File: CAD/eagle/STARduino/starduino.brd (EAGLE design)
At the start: 101.6 x 38.1 mm, 119 parts, among them J1 J30J-9J30, J2 MICRO_SD, J3 J30J-15J30, J4 J30J-31J30, J5 RPI-ZERO, J6 RPI-CSI, Q1 FDG8842CZ, Q2 FDG8842CZ, Q5 FDG8842CZ, Q6 FDG8842CZ, T1 750313972, U1 LT8301, U10 MC74VHC1GT125, U11 TCA9535_RTW_24, U12 MAX31725MTA+, U13 BMX055, U14 DRV8846RGER, U15 P82B715, U16 MC74VHC1GT125, U17 PCA9306DCT, U2 LT3465/A, U3 LTC3112FE, U4 DS3231MZ+, U5 MT25QL01GBBB8ESF-0AAT, U6 ATSAMD21G18, U7 MIC5319, U8 ADXL375BCCZ, U9 MC14504BDTG

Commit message: Adjusted some STARduino things
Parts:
- removed R20, R21, R33, R36: 4.7k, resistor:R0603
- added C28: 100nF, resistor:C0603
- added R15: 4.7k, SparkFun-Passives:0603-ARV
- C29: value 4.7uF -> 2.2uF; device resistor:A/3216-18R -> resistor:C0603
- moved C29 62.3 mm to (-10.2, -21.6), turned to 0 degrees
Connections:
- removed net N$1: L3.2, U6.44
- removed net N$2: L4.2, U6.17
- removed net N$3: L5.2, U6.36
- removed net N$4: FB1.2, U6.6
- new net N$10: C19.1, C20.1, C21.1, C22.1, C23.1, C24.1, FB1.2, L3.2, L4.2, L5.2, U6.17, U6.36, U6.44, U6.6
- new net N$9: C28.1, U7.4
- net +3V3: now also C29.1, R15.5, R15.6, R15.7, R15.8; no longer C19.1, C20.1, C21.1, C22.1, C23.1, C24.1, C29.+, R20.2, R21.2, R33.2, R36.2
- net GND: now also C28.2, C29.2; no longer C29.-
- net SCL: now also R15.4; no longer R21.1
- net SCL_BUFF: now also R15.2; no longer R36.1
- net SDA: now also R15.3; no longer R20.1
- net SDA_BUFF: now also R15.1; no longer R33.1
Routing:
- net +3V3: track 259.2 -> 246.5 mm
- net N$4: track 9.40 -> 0.00 mm
- net N$2: track 7.24 -> 0.00 mm, vias 2 -> 0
- net SDA: track 117.0 -> 114.0 mm
- net N$1: track 2.90 -> 0.00 mm
- net N$10: track 0.00 -> 2.04 mm
- net GND: track 71.8 -> 70.5 mm, vias 69 -> 68
- net N$3: track 1.09 -> 0.00 mm
- net SCL: track 136.9 -> 135.9 mm
- net SDA_BUFF: track 52.9 -> 52.1 mm
- net SCL_BUFF: track 51.8 -> 51.0 mm

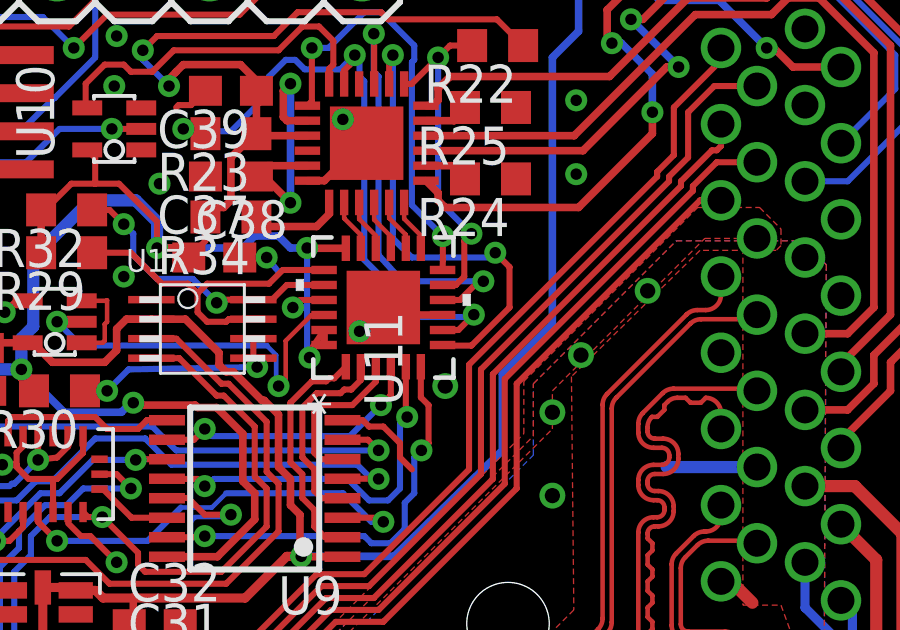
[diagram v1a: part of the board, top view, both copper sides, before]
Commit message: Multiplexer Pinout Change
Small change to multiplexer layout for increased sense-making.
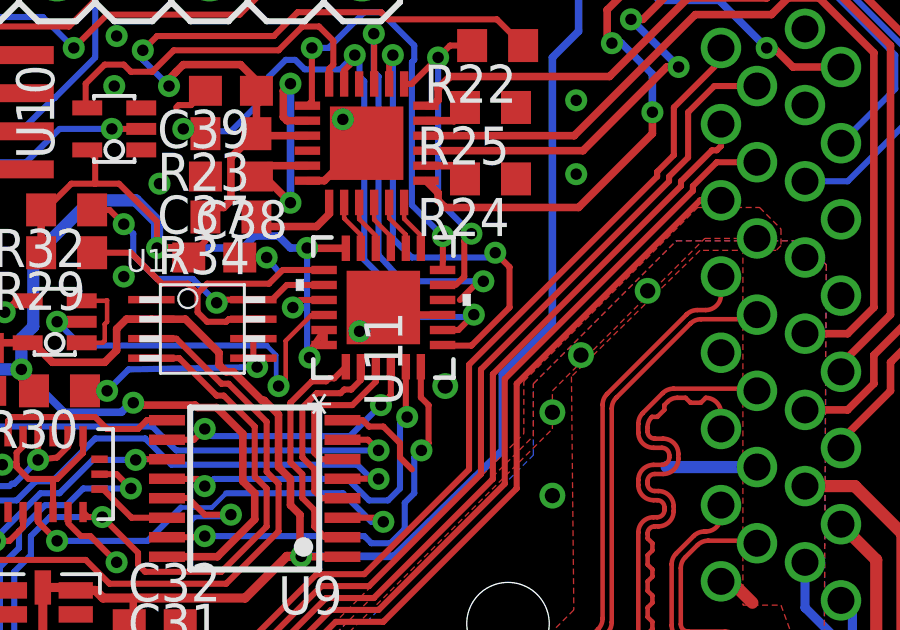
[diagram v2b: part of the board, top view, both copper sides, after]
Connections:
- net M0: now also U11.11; no longer U11.7
- net NFAULT: now also U11.7; no longer U11.11
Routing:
- net M1: track 14.7 -> 14.0 mm
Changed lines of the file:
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@@
 <?xml version="1.0" encoding="utf-8"?>
 <!DOCTYPE eagle SYSTEM "eagle.dtd">
-<eagle version="6.5.0">
+<eagle version="7.5.0">
 <drawing>
 <settings>
@@
 <pass name="Default">
 <param name="RoutingGrid" value="50mil"/>
+<param name="AutoGrid" value="1"/>
+<param name="Efforts" value="0"/>
+<param name="TopRouterVariant" value="1"/>
 <param name="tpViaShape" value="round"/>
 <param name="PrefDir.1" value="|"/>
@@
 <contactref element="U14" pad="7"/>
 <contactref element="R22" pad="2"/>
-<contactref element="U11" pad="11"/>
 <via x="84.93125" y="24.28875" extent="1-16" drill="0.381"/>
 <via x="83.82" y="30.1625" extent="1-16" drill="0.381"/>
 <wire x1="83.82" y1="30.1625" x2="83.82" y2="25.4" width="0.2032" layer="16"/>
 <wire x1="83.82" y1="25.4" x2="84.93125" y2="24.28875" width="0.2032" layer="16"/>
-<wire x1="83.969375" y1="22.5783125" x2="83.9351875" y2="22.5783125" width="0.2032" layer="1"/>
 <wire x1="82.68875" y1="29.28" x2="82.9375" y2="29.28" width="0.2032" layer="1"/>
 <wire x1="82.9375" y1="29.28" x2="83.82" y2="30.1625" width="0.2032" layer="1"/>
 <wire x1="83.82" y1="30.1625" x2="84.216875" y2="30.559375" width="0.2032" layer="1"/>
 <wire x1="84.216875" y1="30.559375" x2="84.954375" y2="30.559375" width="0.2032" layer="1"/>
-<wire x1="83.969375" y1="22.5783125" x2="84.4114375" y2="22.5783125" width="0.2032" layer="1"/>
 <wire x1="84.4114375" y1="22.5783125" x2="84.693125" y2="22.86" width="0.2032" layer="1"/>
 <wire x1="84.693125" y1="22.86" x2="84.693125" y2="24.050625" width="0.2032" layer="1"/>
 <wire x1="84.693125" y1="24.050625" x2="84.93125" y2="24.28875" width="0.2032" layer="1"/>
+<contactref element="U11" pad="7"/>
+<wire x1="83.969375" y1="20.577809375" x2="84.4114375" y2="22.5783125" width="0" layer="19" extent="1-1"/>
 </signal>
 <signal name="SDA">
@@
 <signal name="M0">
 <contactref element="U14" pad="8"/>
-<contactref element="U11" pad="7"/>
 <wire x1="82.18875" y1="29.28" x2="82.18875" y2="30.11875" width="0.2032" layer="1"/>
 <wire x1="82.18875" y1="30.11875" x2="82.311875" y2="30.241875" width="0.2032" layer="1"/>
@@
 <wire x1="85.56625" y1="23.495" x2="85.725" y2="23.65375" width="0.2032" layer="16"/>
 <wire x1="84.058125" y1="20.558125" x2="84.038440625" y2="20.577809375" width="0.2032" layer="1"/>
-<wire x1="84.038440625" y1="20.577809375" x2="83.969375" y2="20.577809375" width="0.2032" layer="1"/>
 <wire x1="82.311875" y1="24.13" x2="82.946875" y2="23.495" width="0.2032" layer="16"/>
 <via x="85.725" y="23.65375" extent="1-16" drill="0.381"/>
@@
 <wire x1="86.20125" y1="21.828125" x2="86.20125" y2="23.1775" width="0.2032" layer="1"/>
 <wire x1="86.20125" y1="23.1775" x2="85.725" y2="23.65375" width="0.2032" layer="1"/>
+<contactref element="U11" pad="11"/>
+<wire x1="83.969375" y1="22.5783125" x2="82.946875" y2="23.495" width="0" layer="19" extent="1-16"/>
 </signal>
 <signal name="M1">
 <contactref element="U14" pad="9"/>
-<contactref element="U11" pad="10"/>
 <wire x1="81.68875" y1="29.28" x2="81.68875" y2="30.865" width="0.2032" layer="1"/>
 <wire x1="81.68875" y1="30.865" x2="81.676875" y2="30.95625" width="0.2032" layer="1"/>
 <via x="81.676875" y="30.95625" extent="1-16" drill="0.381"/>
 <via x="85.328125" y="22.70125" extent="1-16" drill="0.381"/>
-<wire x1="83.8874375" y1="22.0781875" x2="83.969375" y2="22.0781875" width="0.2032" layer="1"/>
 <wire x1="81.676875" y1="30.95625" x2="81.676875" y2="29.68625" width="0.2032" layer="16"/>
 <wire x1="81.676875" y1="29.68625" x2="81.835625" y2="29.5275" width="0.2032" layer="16"/>
@@
 <wire x1="81.835625" y1="23.574375" x2="82.629375" y2="22.70125" width="0.2032" layer="16"/>
 <wire x1="82.629375" y1="22.70125" x2="85.328125" y2="22.70125" width="0.2032" layer="16"/>
-<wire x1="83.969375" y1="22.0781875" x2="84.5463125" y2="22.0781875" width="0.2032" layer="1"/>
 <wire x1="84.5463125" y1="22.0781875" x2="85.169375" y2="22.70125" width="0.2032" layer="1"/>
 <wire x1="85.169375" y1="22.70125" x2="85.328125" y2="22.70125" width="0.2032" layer="1"/>
+<contactref element="U11" pad="10"/>
+<wire x1="84.5463125" y1="22.0781875" x2="83.969375" y2="22.0781875" width="0" layer="19" extent="1-1"/>
 </signal>
 <signal name="N$22">

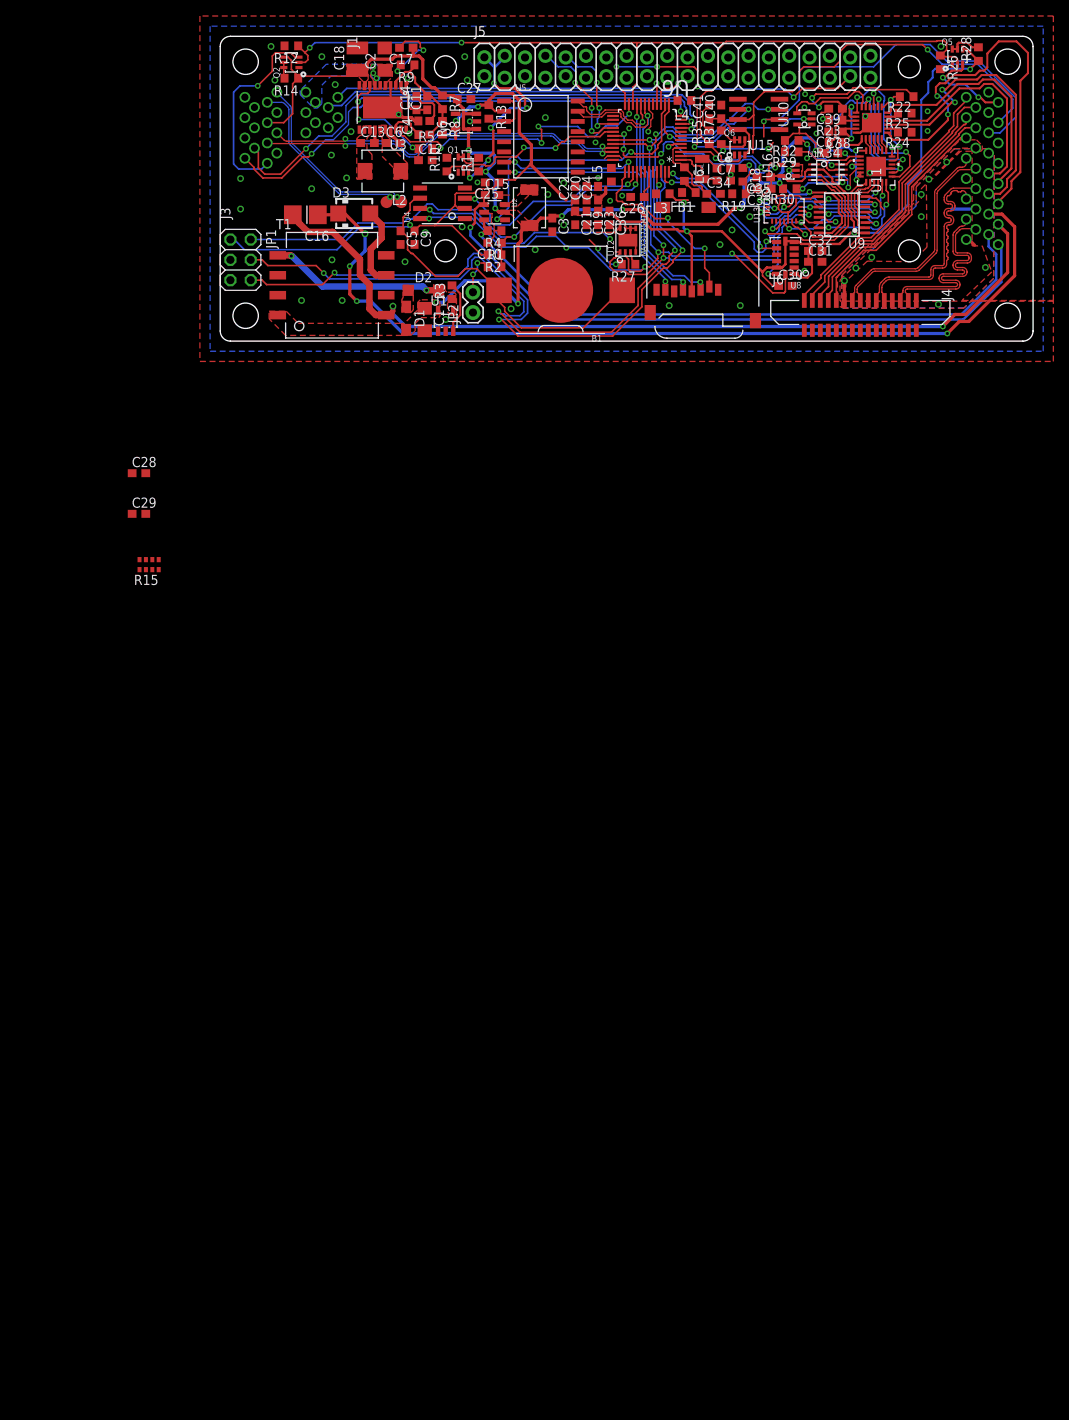
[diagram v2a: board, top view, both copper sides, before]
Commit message: STARduino progress. De-stupified 28V bias
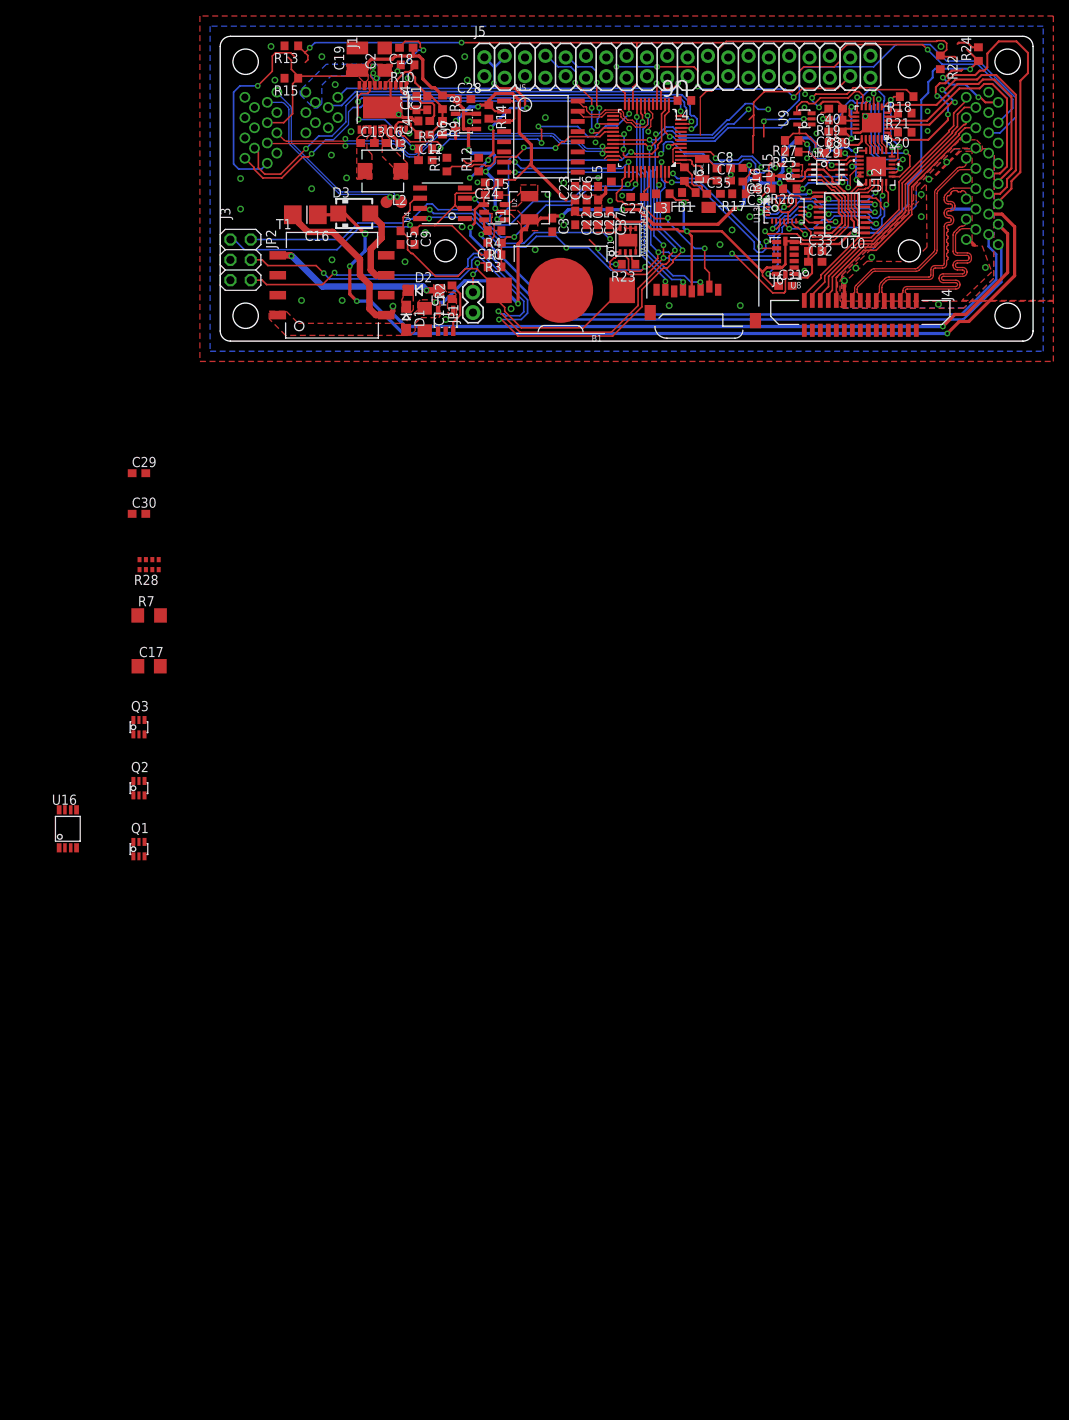
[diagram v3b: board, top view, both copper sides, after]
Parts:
- removed C41: 100nF, resistor:C0603
- removed Q5, Q6: FDG8842CZ, NR_Transistor:SC-70-6
- removed R30: 220k, rcl:R0603
- removed R32: 4.7k, rcl:R0603
- removed R34: 10k, rcl:R0603
- removed R35: 100k, resistor:R0603
- removed R37: 191k, resistor:R0603
- added Q3: BSS8402DW, transistor-fet:SC70
- added R16: 3.6k, resistor:R0603
- added R17: 6.8k, resistor:R0603
- added R20, R21: 1.05, rcl:R0603
- C17: value 47pF -> 3.3nF; device resistor:C0603 -> resistor:C1206
- C18: value 47uF -> 47pF; device resistor:C1210 -> resistor:C0603
- C19: value 10uF -> 47uF; device resistor:C0603 -> resistor:C1210
- C21, C31, C39: value 100nF -> 10uF
- C26: value 1uF -> 100nF
- C28: value 100nF -> 1uF
- C29: value 2.2uF -> 100nF
- C30, C38: value 10uF -> 2.2uF
- C37: value 2.2uF -> 100nF; device rcl:C0603 -> resistor:C0603
- C40: value 1uF -> 100nF; device resistor:C0603 -> rcl:C0603
- D1: value CMDZ5257B -> CMDZ5248B
- JP1: device pinhead:2X03 -> CM_passives:1X02
- JP2: device CM_passives:1X02 -> pinhead:2X03
- Q1, Q2: value FDG8842CZ -> BSS8402DW; device NR_Transistor:SC-70-6 -> transistor-fet:SC70
- R10: value 100k -> 10k
- R11: value 191k -> 100k
- R12: value 100k -> 191k
- R13: value 4.7k -> 100k
- R14: value 191k -> 4.7k
- R15: value 4.7k -> 191k; device SparkFun-Passives:0603-ARV -> resistor:R0603
- R18: value 3.6k -> 10k; device resistor:R0603 -> rcl:R0603
- R19: value 6.8k -> 10k; device resistor:R0603 -> rcl:R0603
- R2: value 10k -> 130k
- R22: value 10k -> 100k; device rcl:R0603 -> resistor:R0603
- R23: value 10k -> 4.7k; device rcl:R0603 -> resistor:R0603
- R24: value 1.05 -> 191k; device rcl:R0603 -> resistor:R0603
- R25: value 1.05 -> 4.7k
- R26: value 100k -> 220k; device resistor:R0603 -> rcl:R0603
- R27: device resistor:R0603 -> rcl:R0603
- R28: value 191k -> 4.7k; device resistor:R0603 -> SparkFun-Passives:0603-ARV
- R29: value 4.7k -> 10k
- R3: value 270k -> 10k
- R7: value 845k -> 1.5k; device resistor:R0603 -> resistor:R1206
- R8: value 158k -> 845k
- R9: value 10k -> 158k
- T1: value 750313972 -> 750313975
- U$1: value SSL.3IN_SILK -> STAR; device images:SSL_SILK_.3IN -> images:STAR_.3IN
- U$2: value STAR -> SSL.3IN_SILK; device images:STAR_.3IN -> images:SSL_SILK_.3IN
- U10: value MC74VHC1GT125 -> MC14504BDTG; device CM_IC:SC-70-5 -> MotorDriver:TSSOP16
- U11: value TCA9535_RTW_24 -> MAX31725MTA+; device MotorDriver:RTW24_2P45X2P45 -> NR_IC:DFN-8
- U12: value MAX31725MTA+ -> TCA9535_RTW_24; device NR_IC:DFN-8 -> MotorDriver:RTW24_2P45X2P45
- U15: value P82B715 -> MC74VHC1GT125; device CM_IC:SO8 -> CM_IC:SC-70-5
- U16: value MC74VHC1GT125 -> PCA9515A; device CM_IC:SC-70-5 -> CM_IC:TSSOP8
- U9: value MC14504BDTG -> MC74VHC1GT125; device MotorDriver:TSSOP16 -> CM_IC:SC-70-5
- moved U16 122.0 mm to (-19.1, -61.0), turned to 0 degrees
- moved R28 121.7 mm to (-8.89, -27.9), turned to 0 degrees
- moved Q1 94.7 mm to (-10.2, -63.5)
- moved Q2 92.7 mm to (-10.2, -55.9), turned to 0 degrees
- moved C30 85.7 mm to (-10.2, -21.6)
- moved C17 83.7 mm to (-8.89, -40.6), turned to 0 degrees
- moved R7 73.9 mm to (-8.89, -34.3), turned to 0 degrees
- moved R15 63.3 mm to (8.89, 32.9), turned to 180 degrees
- moved C28 61.9 mm to (30.5, 30.2)
- moved C19 34.9 mm to (17.1, 35.2), turned to 90 degrees
- moved U11 32.4 mm to (51.0, 12.6)
- moved U12 32.4 mm to (82.0, 21.8)
- moved R23 31.5 mm to (51.0, 9.60)
- moved C37 30.2 mm to (48.7, 15.4), turned to 270 degrees
- moved JP1 29.8 mm to (31.6, 3.57), turned to 90 degrees
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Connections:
- removed net N$17: Q6.5, Q6.6, R37.2
- removed net N$36: C40.1, C41.1, Q6.3, U15.8
- net +3V3: now also C24.1, C34.1, C37.1, JP2.1, Q3.4, R14.1, R23.2, R24.1, R28.5, R28.6, R28.7, R28.8, R3.2, U10.1, U11.8, U15.5, U16.P$8; no longer C25.1, C29.1, C35.1, JP1.1, Q5.4, Q6.4, R13.1, R15.5, R15.6, R15.7, R15.8, R2.2, R27.2, R28.1, R37.1, U12.8, U16.5, U9.1
- net +5V: now also C19.1, C28.1, C40.1, R12.1, R15.1, R16.1, R19.1, R25.2, R26.2, R27.2, R8.1, U10.16, U12.18, U12.21, U12.23, U12.24, U9.5; no longer C17.1, C27.1, C38.1, R11.1, R14.1, R22.1, R23.1, R30.2, R32.2, R34.2, R7.1, U10.5, U11.18, U11.21, U11.23, U11.24, U9.16
- net BIAS_GND: now also C17.1, R7.1, T1.7
- net BIAS_V: now also R7.2
- net DEC0: now also U12.15; no longer U11.15
- net DEC1: now also U12.13; no longer U11.13
- net DIR: now also U12.12; no longer U11.12
- net EXTERNAL_3V3: now also Q3.3; no longer Q5.3
- net EXTERNAL_KILL: now also Q3.2, R13.1, R22.1, U16.P$5; no longer Q5.2, Q6.2, R12.1, R26.1, R35.1
- net FB_5: now also R10.1, R8.2; no longer R7.2, R8.1
- net GND: now also C17.2, JP1.1, JP2.5, Q3.1, R11.2, R13.2, R17.2, R20.1, R21.1, R22.2, R9.2, U10.13, U10.8, U11.4, U11.5, U11.6, U11.7, U12.25, U15.1, U15.3, U9.1, U9.3; no longer C18.2, C41.2, JP1.5, JP2.1, Q5.1, Q6.1, R10.2, R12.2, R19.2, R24.1, R25.1, R26.2, R35.2, R8.2, U10.1, U10.3, U11.25, U12.4, U12.5, U12.6, U12.7, U15.4, U16.1, U16.3, U9.13, U9.8
- net I0: now also U12.17; no longer U11.17
- net I1: now also U12.16; no longer U11.16
- net IMUDR: now also U10.9; no longer U9.9
- net IMUINT1: now also U10.5; no longer U9.5
- net IMUINT2: now also U10.7; no longer U9.7
- net IMUINT3: now also U10.3; no longer U9.3
- net IMUINT4: now also U10.11; no longer U9.11
- net IMUINT5: now also U10.14; no longer U9.14
- net IOEINT: now also U15.4; no longer U16.4
- net M0: now also U12.11; no longer U11.11
- net M1: now also U12.10; no longer U11.10
- net N$10: now also C25.1, C26.1; no longer C19.1, C24.1
- net N$16: now also R29.1; no longer R34.1
- net N$18: now also Q3.5, Q3.6, R24.2; no longer Q5.5, Q5.6, R28.2
- net N$19: now also U10.2, U12.1; no longer U11.1, U9.2
- net N$20: now also R21.2; no longer R25.2
- net N$21: now also R20.2; no longer R24.2
- net N$22: now also U9.4; no longer U10.4
- net N$23: now also U10.4, U12.2; no longer U11.2, U9.4
- net N$25: now also U12.22, U15.2; no longer U11.22, U16.2
- net N$26: now also C38.1; no longer C37.1
- net N$28: now also U10.6, U12.3; no longer U11.3, U9.6
- net N$29: now also U10.10, U12.4; no longer U11.4, U9.10
- net N$30: now also U10.12, U12.5; no longer U11.5, U9.12
- net N$31: now also U10.15, U12.6; no longer U11.6, U9.15
- net N$32: now also R14.2; no longer R13.2
- net N$33: now also R27.1, U12.20; no longer R32.1, U11.20
- net N$34: now also R25.1, U12.19; no longer R29.1, U11.19
- net N$35: now also R26.1; no longer R30.1
- net N$37: now also R12.2; no longer R11.2
- net N$38: now also R15.2; no longer R14.2
- net N$48: now also C18.2, R10.2; no longer C17.2, R9.2
- net N$49: now also R2.2; no longer R3.2
- net N$5: now also C27.1; no longer C26.1
- net N$50: now also R2.1; no longer R3.1
- net N$52: now also T1.5
- net N$6: now also R23.1, U11.3; no longer R27.1, U12.3
- net N$7: now also JP1.2; no longer JP2.2
- net N$9: now also C29.1; no longer C28.1
- net NENBL: now also R19.2, U12.8; no longer R23.2, U11.8
- net NFAULT: now also R18.2, U12.7; no longer R22.2, U11.7
- net NSLEEP: now also U12.14; no longer U11.14
- net PI_KILL: now also R11.1; no longer R10.1
- net RESET: now also JP2.2, R3.1; no longer JP1.2, R2.1
- net SCL: now also R28.4, U11.2; no longer R15.4, U12.2, U15.3
- net SCL_BUFF: now also R28.2; no longer R15.2, U15.2
- net SDA: now also R28.3, U11.1; no longer R15.3, U12.1, U15.6
- net SDA_BUFF: now also R28.1; no longer R15.1, U15.7
- net STEPFREQ: now also U9.2; no longer U10.2
- net SWDCLK: now also JP2.4; no longer JP1.4
- net SWDIO: now also JP2.6; no longer JP1.6
- net VREFA: now also C35.1; no longer C34.1
- net V_SENSE: now also R16.2, R17.1; no longer R18.2, R19.1
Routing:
- net +3V3: track 246.5 -> 225.0 mm, vias 14 -> 11
- net EXTERNAL_KILL: track 117.6 -> 108.9 mm
- net N$36: track 8.58 -> 0.00 mm
- net GND: track 70.5 -> 66.6 mm
- net N$17: track 2.81 -> 0.00 mm
- net N$38: track 2.03 -> 0.14 mm
- net SCL_BUFF: track 51.0 -> 49.2 mm
- net SDA_BUFF: track 52.1 -> 50.7 mm
- net SCL: track 135.9 -> 134.5 mm
- net SDA: track 114.0 -> 112.7 mm
- net N$18: track 4.21 -> 2.92 mm
- net N$37: track 3.46 -> 2.42 mm
- net +5V: track 202.0 -> 201.2 mm
- net PI_KILL: track 24.2 -> 23.4 mm
- net EXTERNAL_3V3: track 11.7 -> 11.1 mm
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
